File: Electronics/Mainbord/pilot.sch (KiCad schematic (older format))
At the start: 26 parts, among them J10 Screw_Terminal_01x10, J11 Screw_Terminal_01x10, J12 Screw_Terminal_01x10, J13 Screw_Terminal_01x10, J14 Screw_Terminal_01x10, J15 Screw_Terminal_01x02, U10 74HC165, U11 74HC165, U12 74HC165, U13 74HC165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

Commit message: Electronics - Misc works
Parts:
- removed J15: Screw_Terminal_01x02, symbol Connector:Screw_Terminal_01x02
- removed R10: 150, symbol Device:R
- added J?: Screw_Terminal_01x10, symbol Connector:Screw_Terminal_01x10
- added R? (x2): 68, symbol Device:R
- added U?: ULN2803A, symbol Transistor_Array:ULN2803A
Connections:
- wire segments 124 -> 157
- no-connect marks 5 -> 6
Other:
- note removed: "The 3.3V leds need a \ncurrent-limiting resistor.\n3.3 V /150 ohms = 22mA\n"
- moved on the sheet: C24, J14, U15

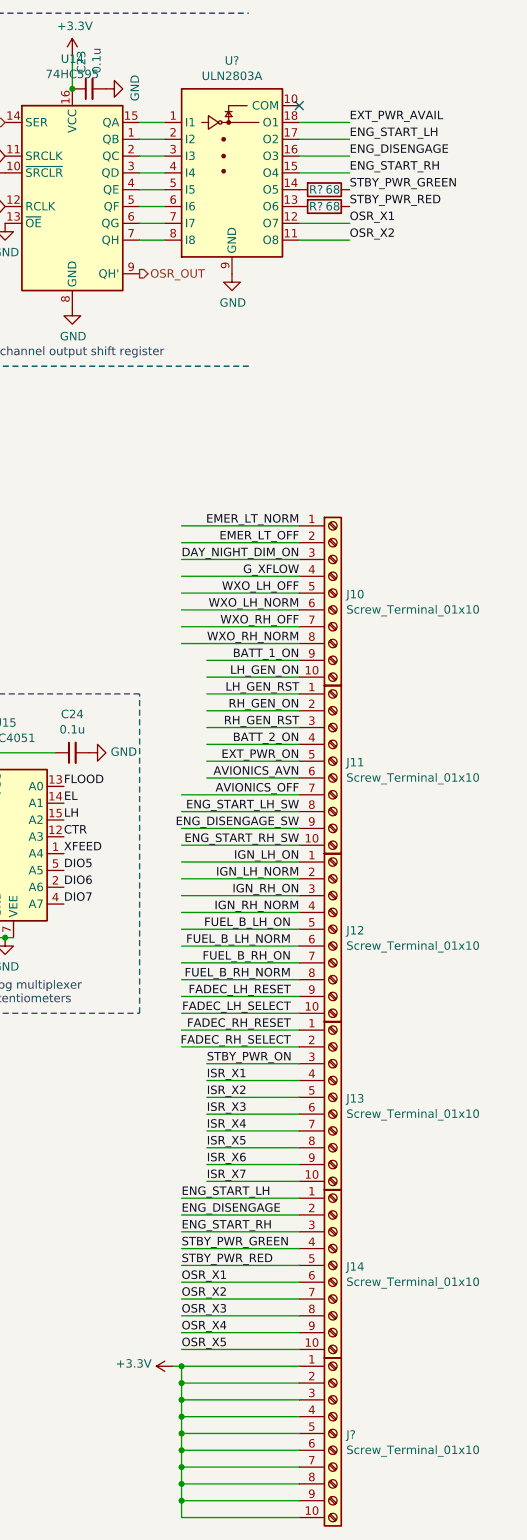
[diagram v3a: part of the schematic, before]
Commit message: Electronics - Adds LCSC part numbers and footprints
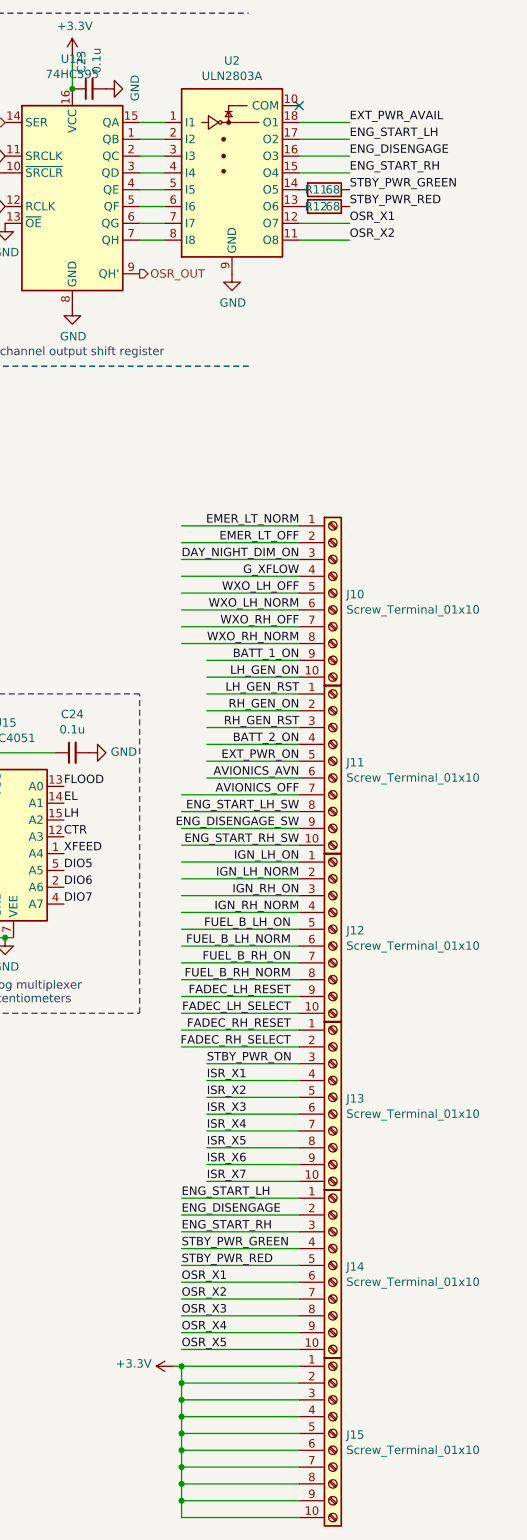
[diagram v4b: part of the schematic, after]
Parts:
- J10, J11, J12, J13, J14: footprint (none) -> Connector_PinSocket_1.27mm:PinSocket_1x10_P1.27mm_Vertical
- J15: renamed from J?; footprint (none) -> Connector_PinSocket_1.27mm:PinSocket_1x10_P1.27mm_Vertical
- U10, U11, U12, U13, U9: footprint (none) -> Package_SO:SOIC-16_3.9x9.9mm_P1.27mm; LCSC (none) -> C5613
- U14: footprint (none) -> Package_SO:SOIC-16_3.9x9.9mm_P1.27mm; LCSC (none) -> C5947
- U15: footprint (none) -> Package_SO:TSSOP-16_4.4x5mm_P0.65mm; LCSC (none) -> C5645
- U2: renamed from U?; footprint (none) -> Package_SO:SOIC-18W_7.5x11.6mm_P1.27mm; LCSC (none) -> C9683
- gave numbers to parts that had none: 2
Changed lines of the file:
@@
 F 0 "U9" H 2750 2547 60  0000 C CNN
 F 1 "74HC165" H 2750 2441 60  0000 C CNN
-F 2 "" H 4940 430 60  0001 C CNN
+F 2 "Package_SO:SOIC-16_3.9x9.9mm_P1.27mm" H 4940 430 60  0001 C CNN
 F 3 "" H 4940 430 60  0001 C CNN
+F 4 "C5613" H 2750 1650 50  0001 C CNN "LCSC"
 	1    2750 1650
 	1    0    0    -1
@@
 F 0 "U10" H 2750 4247 60  0000 C CNN
 F 1 "74HC165" H 2750 4141 60  0000 C CNN
-F 2 "" H 4940 2130 60  0001 C CNN
+F 2 "Package_SO:SOIC-16_3.9x9.9mm_P1.27mm" H 4940 2130 60  0001 C CNN
 F 3 "" H 4940 2130 60  0001 C CNN
+F 4 "C5613" H 2750 3350 50  0001 C CNN "LCSC"
 	1    2750 3350
 	1    0    0    -1
@@
 F 0 "U11" H 2750 5947 60  0000 C CNN
 F 1 "74HC165" H 2750 5841 60  0000 C CNN
-F 2 "" H 4940 3830 60  0001 C CNN
+F 2 "Package_SO:SOIC-16_3.9x9.9mm_P1.27mm" H 4940 3830 60  0001 C CNN
 F 3 "" H 4940 3830 60  0001 C CNN
+F 4 "C5613" H 2750 5050 50  0001 C CNN "LCSC"
 	1    2750 5050
 	1    0    0    -1
@@
 F 0 "U12" H 2750 7647 60  0000 C CNN
 F 1 "74HC165" H 2750 7541 60  0000 C CNN
-F 2 "" H 4940 5530 60  0001 C CNN
+F 2 "Package_SO:SOIC-16_3.9x9.9mm_P1.27mm" H 4940 5530 60  0001 C CNN
 F 3 "" H 4940 5530 60  0001 C CNN
+F 4 "C5613" H 2750 6750 50  0001 C CNN "LCSC"
 	1    2750 6750
 	1    0    0    -1
@@
 F 0 "U13" H 2750 9347 60  0000 C CNN
 F 1 "74HC165" H 2750 9241 60  0000 C CNN
-F 2 "" H 4940 7230 60  0001 C CNN
+F 2 "Package_SO:SOIC-16_3.9x9.9mm_P1.27mm" H 4940 7230 60  0001 C CNN
 F 3 "" H 4940 7230 60  0001 C CNN
+F 4 "C5613" H 2750 8450 50  0001 C CNN "LCSC"
 	1    2750 8450
 	1    0    0    -1
@@
 F 0 "U14" H 5150 2328 50  0000 C CNN
 F 1 "74HC595" H 5150 2237 50  0000 C CNN
-F 2 "" H 5150 1550 50  0001 C CNN
+F 2 "Package_SO:SOIC-16_3.9x9.9mm_P1.27mm" H 5150 1550 50  0001 C CNN
 F 3 "http://www.ti.com/lit/ds/symlink/sn74hc595.pdf" H 5150 1550 50  0001 C CNN
+F 4 "C5947" H 5150 1550 50  0001 C CNN "LCSC"
 	1    5150 1550
 	1    0    0    -1
@@
 F 0 "J10" H 6780 3942 50  0000 L CNN
 F 1 "Screw_Terminal_01x10" H 6780 3851 50  0000 L CNN
-F 2 "" H 6700 3950 50  0001 C CNN
+F 2 "Connector_PinSocket_1.27mm:PinSocket_1x10_P1.27mm_Vertical" H 6700 3950 50  0001 C CNN
 F 3 "~" H 6700 3950 50  0001 C CNN
 	1    6700 3950
@@
 F 0 "J11" H 6780 4942 50  0000 L CNN
 F 1 "Screw_Terminal_01x10" H 6780 4851 50  0000 L CNN
-F 2 "" H 6700 4950 50  0001 C CNN
+F 2 "Connector_PinSocket_1.27mm:PinSocket_1x10_P1.27mm_Vertical" H 6700 4950 50  0001 C CNN
 F 3 "~" H 6700 4950 50  0001 C CNN
 	1    6700 4950
@@
 F 0 "J12" H 6780 5942 50  0000 L CNN
 F 1 "Screw_Terminal_01x10" H 6780 5851 50  0000 L CNN
-F 2 "" H 6700 5950 50  0001 C CNN
+F 2 "Connector_PinSocket_1.27mm:PinSocket_1x10_P1.27mm_Vertical" H 6700 5950 50  0001 C CNN
 F 3 "~" H 6700 5950 50  0001 C CNN
 	1    6700 5950
@@
 F 0 "J13" H 6780 6942 50  0000 L CNN
 F 1 "Screw_Terminal_01x10" H 6780 6851 50  0000 L CNN
-F 2 "" H 6700 6950 50  0001 C CNN
+F 2 "Connector_PinSocket_1.27mm:PinSocket_1x10_P1.27mm_Vertical" H 6700 6950 50  0001 C CNN
 F 3 "~" H 6700 6950 50  0001 C CNN
 	1    6700 6950
@@
 F 0 "J14" H 6780 7942 50  0000 L CNN
 F 1 "Screw_Terminal_01x10" H 6780 7851 50  0000 L CNN
-F 2 "" H 6700 7950 50  0001 C CNN
+F 2 "Connector_PinSocket_1.27mm:PinSocket_1x10_P1.27mm_Vertical" H 6700 7950 50  0001 C CNN
 F 3 "~" H 6700 7950 50  0001 C CNN
 	1    6700 7950
@@
 F 0 "U15" H 4750 6078 50  0000 C CNN
 F 1 "74HC4051" H 4750 5987 50  0000 C CNN
-F 2 "" H 4700 5000 50  0001 C CNN
+F 2 "Package_SO:TSSOP-16_4.4x5mm_P0.65mm" H 4700 5000 50  0001 C CNN
 F 3 "http://www.ti.com/lit/ds/symlink/cd74hc4051.pdf" H 4700 5000 50  0001 C CNN
+F 4 "C5645" H 4700 5400 50  0001 C CNN "LCSC"
 	1    4700 5400
 	1    0    0    -1
@@
 AR Path="/5DC174D4/5DF7511E" Ref="U?"  Part="1"
 AR Path="/5DC2EEA6/5DF7511E" Ref="U?"  Part="1"
-AR Path="/5DB5DCD1/5DF7511E" Ref="U?"  Part="1"
-F 0 "U?" H 6100 1917 50  0000 C CNN
+AR Path="/5DB5DCD1/5DF7511E" Ref="U2"  Part="1"
+F 0 "U2" H 6100 1917 50  0000 C CNN
 F 1 "ULN2803A" H 6100 1826 50  0000 C CNN
-F 2 "" H 6150 700 50  0001 L CNN
+F 2 "Package_SO:SOIC-18W_7.5x11.6mm_P1.27mm" H 6150 700 50  0001 L CNN
 F 3 "http://www.ti.com/lit/ds/symlink/uln2803a.pdf" H 6200 1150 50  0001 C CNN
+F 4 "C9683" H 6100 1350 50  0001 C CNN "LCSC"
 	1    6100 1350
 	1    0    0    -1
 $EndComp
 $Comp
-L power:GND #PWR?
+L power:GND #PWR0152
 U 1 1 5DF75125
 P 6100 2050
-AR Path="/5DB5DCD1/5DF75125" Ref="#PWR?"  Part="1"
+AR Path="/5DB5DCD1/5DF75125" Ref="#PWR0152"  Part="1"
 AR Path="/5DC174D4/5DF75125" Ref="#PWR?"  Part="1"
 AR Path="/5DC31399/5DF75125" Ref="#PWR?"  Part="1"
 AR Path="/5DC2EEA6/5DF75125" Ref="#PWR?"  Part="1"
-F 0 "#PWR?" H 6100 1800 50  0001 C CNN
+F 0 "#PWR0152" H 6100 1800 50  0001 C CNN
 F 1 "GND" H 6105 1877 50  0000 C CNN
 F 2 "" H 6100 2050 50  0001 C CNN
@@
 AR Path="/5DC174D4/5DF75140" Ref="R?"  Part="1"
 AR Path="/5DC2EEA6/5DF75140" Ref="R?"  Part="1"
-AR Path="/5DB5DCD1/5DF75140" Ref="R?"  Part="1"
-F 0 "R?" V 6650 1500 50  0000 C CNN
+AR Path="/5DB5DCD1/5DF75140" Ref="R11"  Part="1"
+F 0 "R11" V 6650 1500 50  0000 C CNN
 F 1 "68" V 6650 1600 50  0000 C CNN
 F 2 "" V 6580 1550 50  0001 C CNN
@@
 AR Path="/5DC174D4/5DFE110D" Ref="R?"  Part="1"
 AR Path="/5DC2EEA6/5DFE110D" Ref="R?"  Part="1"
-AR Path="/5DB5DCD1/5DFE110D" Ref="R?"  Part="1"
-F 0 "R?" V 6650 1600 50  0000 C CNN
+AR Path="/5DB5DCD1/5DFE110D" Ref="R12"  Part="1"
+F 0 "R12" V 6650 1600 50  0000 C CNN
 F 1 "68" V 6650 1700 50  0000 C CNN
 F 2 "" V 6580 1650 50  0001 C CNN
@@
 	6500 1850 6800 1850
 $Comp
-L Connector:Screw_Terminal_01x10 J?
+L Connector:Screw_Terminal_01x10 J15
 U 1 1 5E003B1A
 P 6700 8950
-F 0 "J?" H 6780 8942 50  0000 L CNN
+F 0 "J15" H 6780 8942 50  0000 L CNN
 F 1 "Screw_Terminal_01x10" H 6780 8851 50  0000 L CNN
-F 2 "" H 6700 8950 50  0001 C CNN
+F 2 "Connector_PinSocket_1.27mm:PinSocket_1x10_P1.27mm_Vertical" H 6700 8950 50  0001 C CNN
 F 3 "~" H 6700 8950 50  0001 C CNN
 	1    6700 8950
@@
 	6500 8550 5800 8550
 $Comp
-L power:+3.3V #PWR?
+L power:+3.3V #PWR0173
 U 1 1 5E01C922
 P 5750 8550
-F 0 "#PWR?" H 5750 8400 50  0001 C CNN
+F 0 "#PWR0173" H 5750 8400 50  0001 C CNN
 F 1 "+3.3V" V 5765 8678 50  0000 L CNN
 F 2 "" H 5750 8550 50  0001 C CNN
